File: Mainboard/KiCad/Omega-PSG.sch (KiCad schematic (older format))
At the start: 14 parts, among them J7 JOYSTICK_A, J8 JOYSTICK_B, U28 74HCT157, U29 74HCT157, U35 74HCT74, U36 74HCT74, U39 74AHCT32, U4 YM2149, U42 74LS07, U44 74AHCT02

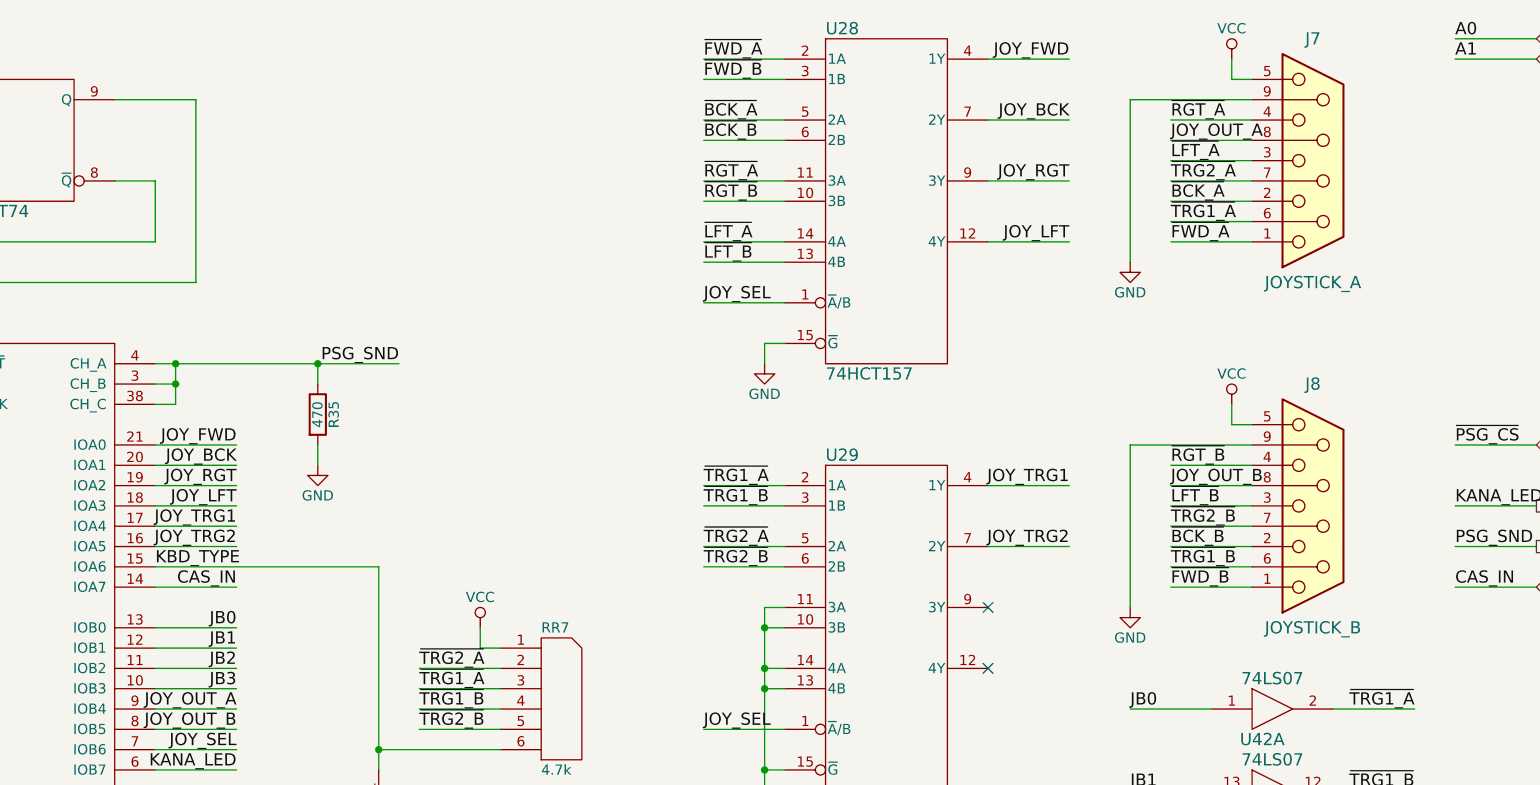
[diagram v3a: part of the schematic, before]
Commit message: Mainboard: Update schematic and PCB layout with latest fixes
Signed-off-by: Sergey Kiselev <skiselev@gmail.com>
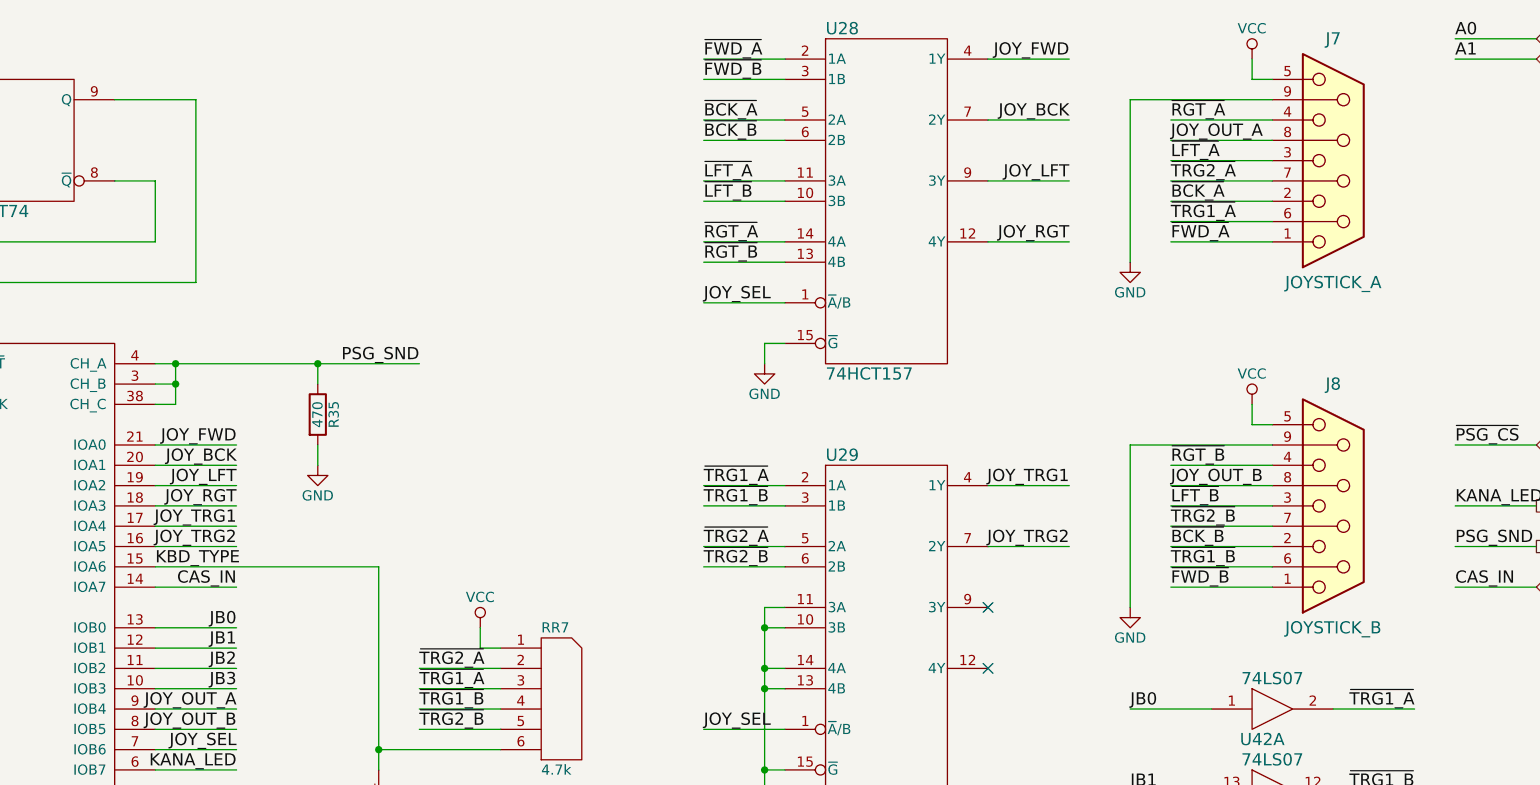
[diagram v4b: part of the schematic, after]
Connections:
- net JOY_LFT: now also U28.9 (3Y), U4.19 (IOA2); no longer U28.12 (4Y), U4.18 (IOA3)
- net JOY_RGT: now also U28.12 (4Y), U4.18 (IOA3); no longer U28.9 (3Y), U4.19 (IOA2)
- net ~LFT_A: now also U28.11 (3A); no longer U28.14 (4A)
- net ~LFT_B: now also U28.10 (3B); no longer U28.13 (4B)
- net ~RGT_A: now also U28.14 (4A); no longer U28.11 (3A)
- net ~RGT_B: now also U28.13 (4B); no longer U28.10 (3B)
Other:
- moved on the sheet: J7, J8
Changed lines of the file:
@@
 Text Label 7200 1100 2    60   ~ 0
 JOY_BCK
-Text Label 7200 1400 2    60   ~ 0
-JOY_RGT
-Text Label 7200 1700 2    60   ~ 0
-JOY_LFT
 Text Label 7200 2900 2    60   ~ 0
 JOY_TRG1
@@
 Text Label 3100 2800 2    60   ~ 0
 JOY_BCK
+Text Label 3100 3000 2    60   ~ 0
+JOY_RGT
 Text Label 3100 2900 2    60   ~ 0
-JOY_RGT
-Text Label 3100 3000 2    60   ~ 0
 JOY_LFT
 Text Label 3100 3100 2    60   ~ 0
@@
 Text Label 5400 1200 0    60   ~ 0
 ~BCK_B
-Text Label 5400 1400 0    60   ~ 0
-~RGT_A
-Text Label 5400 1500 0    60   ~ 0
-~RGT_B
-Text Label 5400 1700 0    60   ~ 0
-~LFT_A
-Text Label 5400 1800 0    60   ~ 0
-~LFT_B
 Text Label 5400 2900 0    60   ~ 0
 ~TRG1_A
@@
 L power:VCC #PWR041
 U 1 1 5A4DDB22
-P 8000 800
-F 0 "#PWR041" H 8000 650 50  0001 C CNN
-F 1 "VCC" H 8000 950 50  0000 C CNN
-F 2 "" H 8000 800 50  0000 C CNN
-F 3 "" H 8000 800 50  0000 C CNN
-	1    8000 800
+P 8100 800
+F 0 "#PWR041" H 8100 650 50  0001 C CNN
+F 1 "VCC" H 8100 950 50  0000 C CNN
+F 2 "" H 8100 800 50  0000 C CNN
+F 3 "" H 8100 800 50  0000 C CNN
+	1    8100 800
 	1    0    0    -1
 $EndComp
@@
 L power:VCC #PWR042
 U 1 1 5A4DDC71
-P 8000 2500
-F 0 "#PWR042" H 8000 2350 50  0001 C CNN
-F 1 "VCC" H 8000 2650 50  0000 C CNN
-F 2 "" H 8000 2500 50  0000 C CNN
-F 3 "" H 8000 2500 50  0000 C CNN
-	1    8000 2500
+P 8100 2500
+F 0 "#PWR042" H 8100 2350 50  0001 C CNN
+F 1 "VCC" H 8100 2650 50  0000 C CNN
+F 2 "" H 8100 2500 50  0000 C CNN
+F 3 "" H 8100 2500 50  0000 C CNN
+	1    8100 2500
 	1    0    0    -1
 $EndComp
@@
 	1    0    0    -1
 $EndComp
-Text Label 3900 2300 2    60   ~ 0
+Text Label 4000 2300 2    60   ~ 0
 PSG_SND
 Text HLabel 9500 3200 2    60   Output ~ 0
@@
 L Connector:DB9_Female J7
 U 1 1 5BF6F401
-P 8400 1300
-F 0 "J7" H 8400 700 60  0000 C CNN
-F 1 "JOYSTICK_A" H 8400 1900 60  0000 C CNN
-F 2 "My_Components:Conn_Dsub_DE9M" H 8400 1300 50  0001 C CNN
-F 3 "" H 8400 1300 50  0001 C CNN
-	1    8400 1300
+P 8500 1300
+F 0 "J7" H 8500 700 60  0000 C CNN
+F 1 "JOYSTICK_A" H 8500 1900 60  0000 C CNN
+F 2 "My_Components:Conn_Dsub_DE9M" H 8500 1300 50  0001 C CNN
+F 3 "" H 8500 1300 50  0001 C CNN
+	1    8500 1300
 	1    0    0    1
 $EndComp
@@
 L Connector:DB9_Female J8
 U 1 1 5BF6F467
-P 8400 3000
-F 0 "J8" H 8400 2400 60  0000 C CNN
-F 1 "JOYSTICK_B" H 8400 3600 60  0000 C CNN
-F 2 "My_Components:Conn_Dsub_DE9M" H 8400 3000 50  0001 C CNN
-F 3 "" H 8400 3000 50  0001 C CNN
-	1    8400 3000
+P 8500 3000
+F 0 "J8" H 8500 2400 60  0000 C CNN
+F 1 "JOYSTICK_B" H 8500 3600 60  0000 C CNN
+F 2 "My_Components:Conn_Dsub_DE9M" H 8500 3000 50  0001 C CNN
+F 3 "" H 8500 3000 50  0001 C CNN
+	1    8500 3000
 	1    0    0    1
 $EndComp
@@
 $EndComp
 Wire Wire Line
-	8100 900  8000 900
-Wire Wire Line
-	8100 1100 7700 1100
-Wire Wire Line
-	8100 1200 7700 1200
-Wire Wire Line
-	8100 1300 7700 1300
-Wire Wire Line
-	8100 1400 7700 1400
-Wire Wire Line
-	8100 1500 7700 1500
-Wire Wire Line
-	8100 1600 7700 1600
-Wire Wire Line
-	8100 1700 7700 1700
-Wire Wire Line
-	8100 2600 8000 2600
-Wire Wire Line
-	8100 2800 7700 2800
-Wire Wire Line
-	8100 2900 7700 2900
-Wire Wire Line
-	8100 3000 7700 3000
-Wire Wire Line
-	8100 3100 7700 3100
-Wire Wire Line
-	8100 3200 7700 3200
-Wire Wire Line
-	8100 3300 7700 3300
-Wire Wire Line
-	8100 3400 7700 3400
+	8200 900  8100 900
+Wire Wire Line
+	8200 1100 7700 1100
+Wire Wire Line
+	8200 1200 7700 1200
+Wire Wire Line
+	8200 1300 7700 1300
+Wire Wire Line
+	8200 1400 7700 1400
+Wire Wire Line
+	8200 1500 7700 1500
+Wire Wire Line
+	8200 1600 7700 1600
+Wire Wire Line
+	8200 1700 7700 1700
+Wire Wire Line
+	8200 2600 8100 2600
+Wire Wire Line
+	8200 2800 7700 2800
+Wire Wire Line
+	8200 2900 7700 2900
+Wire Wire Line
+	8200 3000 7700 3000
+Wire Wire Line
+	8200 3100 7700 3100
+Wire Wire Line
+	8200 3200 7700 3200
+Wire Wire Line
+	8200 3300 7700 3300
+Wire Wire Line
+	8200 3400 7700 3400
 Wire Wire Line
 	6800 800  7200 800
@@
 	5800 1200 5400 1200
 Wire Wire Line
-	5800 1400 5400 1400
-Wire Wire Line
-	5800 1500 5400 1500
-Wire Wire Line
-	5800 1700 5400 1700
-Wire Wire Line
-	5800 1800 5400 1800
-Wire Wire Line
 	5800 2200 5700 2200
 Wire Wire Line
@@
 	5700 2200 5700 2300
 Wire Wire Line
-	8000 900  8000 800
-Wire Wire Line
-	8000 2600 8000 2500
+	8100 900  8100 800
+Wire Wire Line
+	8100 2600 8100 2500
 Wire Wire Line
 	7500 3500 7500 2700
 Wire Wire Line
-	7500 2700 8100 2700
-Wire Wire Line
-	8100 1000 7500 1000
+	7500 2700 8200 2700
+Wire Wire Line
+	8200 1000 7500 1000
 Wire Wire Line
 	7500 1000 7500 1800
@@
 	2800 2300 3500 2300
 Wire Wire Line
-	3500 2300 3900 2300
+	3500 2300 4000 2300
 Wire Wire Line
 	1900 7400 3350 7400
@@
 Wire Wire Line
 	1500 1100 1100 1100
+Text Label 7200 1400 2    60   ~ 0
+JOY_LFT
+Text Label 7200 1700 2    60   ~ 0
+JOY_RGT
+Wire Wire Line
+	5800 1500 5400 1500
+Wire Wire Line
+	5800 1400 5400 1400
+Text Label 5400 1500 0    60   ~ 0
+~LFT_B
+Text Label 5400 1400 0    60   ~ 0
+~LFT_A
+Wire Wire Line
+	5800 1800 5400 1800
+Wire Wire Line
+	5800 1700 5400 1700
+Text Label 5400 1800 0    60   ~ 0
+~RGT_B
+Text Label 5400 1700 0    60   ~ 0
+~RGT_A
 $EndSCHEMATC

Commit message: Mainboard: Replace RGB and Cassette connectors with DIN8
Signed-off-by: Sergey Kiselev <skiselev@gmail.com>
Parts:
- renumbered R35 to R37
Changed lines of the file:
@@
 A0
 $Comp
-L Device:R R35
+L Device:R R37
 U 1 1 5BF6213A
 P 3500 2550
-F 0 "R35" V 3580 2550 50  0000 C CNN
+F 0 "R37" V 3580 2550 50  0000 C CNN
 F 1 "470" V 3500 2550 50  0000 C CNN
 F 2 "My_Components:Res_762" V 3430 2550 50  0001 C CNN
